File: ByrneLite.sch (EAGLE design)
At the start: 22 parts, among them J1 5V Reg, U1 TINY85, U2 S108T02, U3 S108T02, U4 S108T02

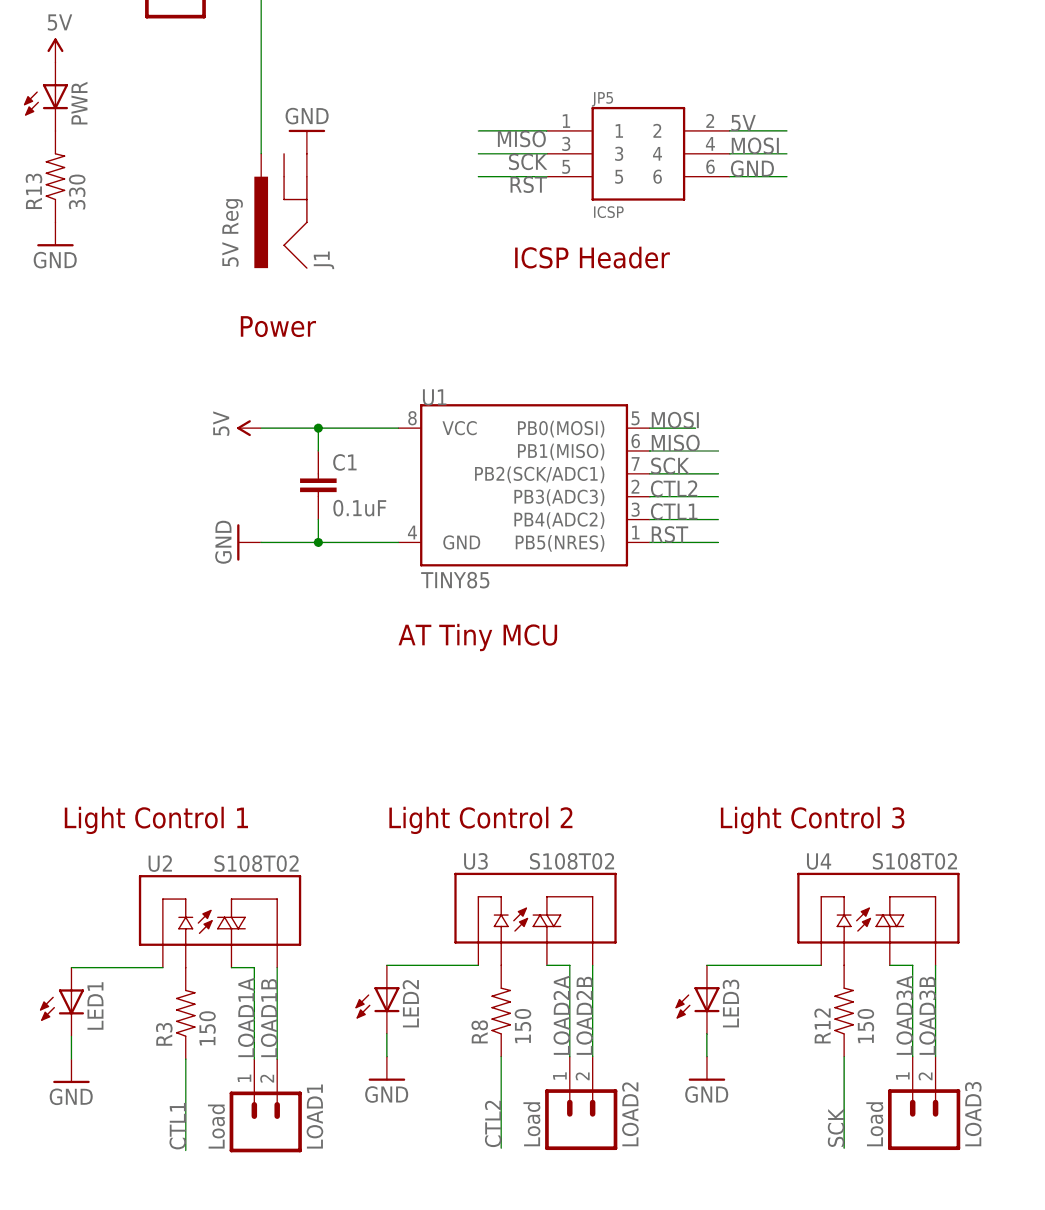
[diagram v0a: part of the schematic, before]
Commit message: Changed to LGPL license
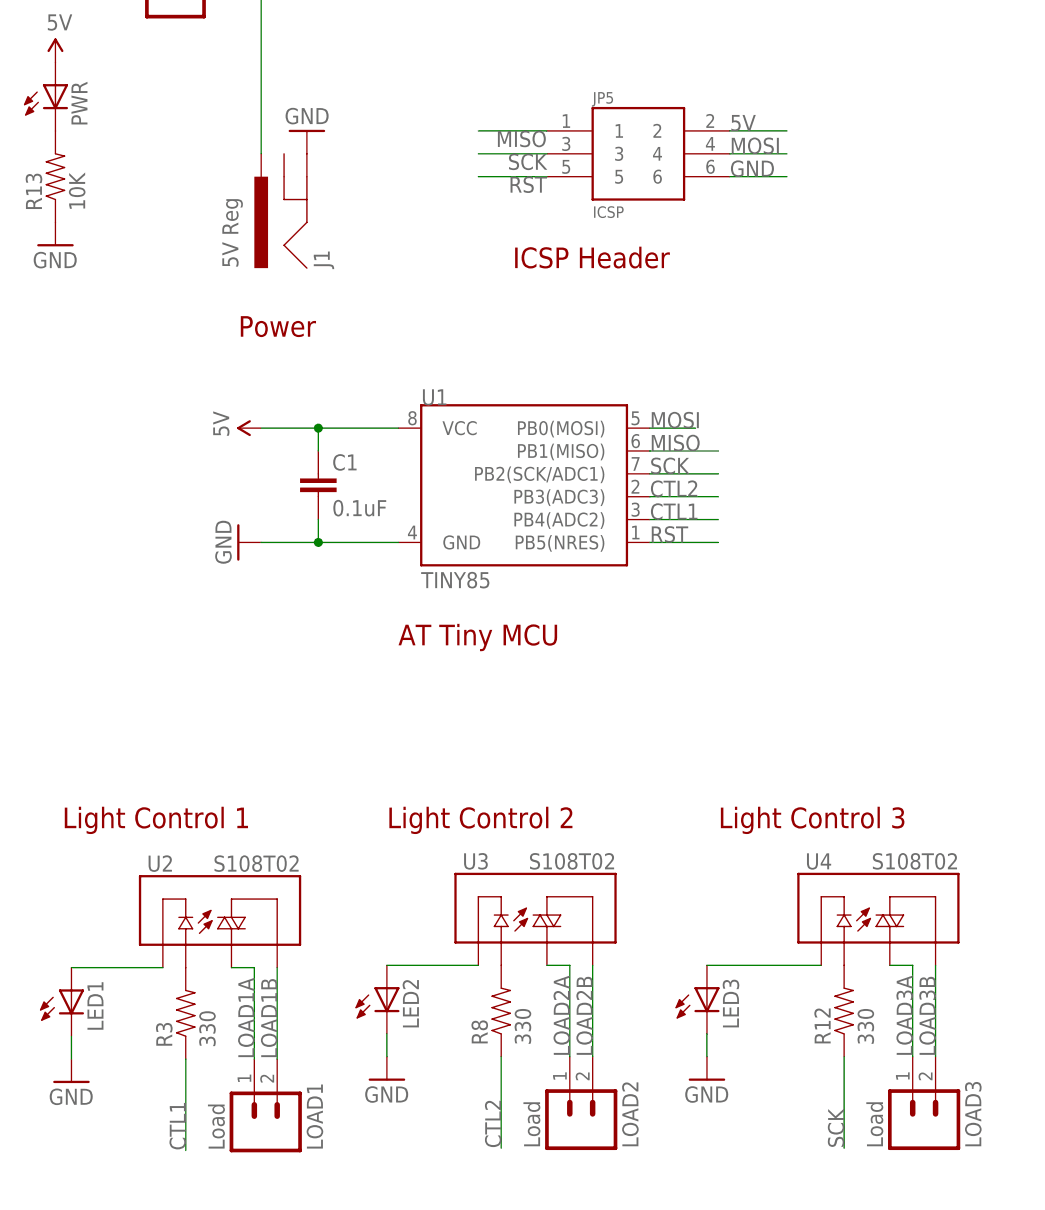
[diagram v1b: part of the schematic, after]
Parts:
- R12, R3, R8: value 150 -> 330
- R13: value 330 -> 10K
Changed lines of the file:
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@@
 <part name="FRAME1" library="SparkFun" deviceset="FRAME-LETTER" device=""/>
 <part name="LED1" library="SparkFun" deviceset="LED" device="5MM"/>
-<part name="R3" library="SparkFun" deviceset="RESISTOR" device="AXIAL-0.3" value="150"/>
+<part name="R3" library="SparkFun" deviceset="RESISTOR" device="AXIAL-0.3" value="330"/>
 <part name="U2" library="SparkFun" deviceset="RELAY-SOLIDSTATE" device="PTH" value="S108T02"/>
 <part name="LOAD1" library="SparkFun" deviceset="M02" device="5MM" value="Load"/>
@@
 <part name="GND2" library="SparkFun" deviceset="GND" device=""/>
 <part name="LED2" library="SparkFun" deviceset="LED" device="5MM"/>
-<part name="R8" library="SparkFun" deviceset="RESISTOR" device="AXIAL-0.3" value="150"/>
+<part name="R8" library="SparkFun" deviceset="RESISTOR" device="AXIAL-0.3" value="330"/>
 <part name="U3" library="SparkFun" deviceset="RELAY-SOLIDSTATE" device="PTH" value="S108T02"/>
 <part name="LOAD2" library="SparkFun" deviceset="M02" device="5MM" value="Load"/>
 <part name="LED3" library="SparkFun" deviceset="LED" device="5MM"/>
 <part name="GND7" library="SparkFun" deviceset="GND" device=""/>
-<part name="R12" library="SparkFun" deviceset="RESISTOR" device="AXIAL-0.3" value="150"/>
+<part name="R12" library="SparkFun" deviceset="RESISTOR" device="AXIAL-0.3" value="330"/>
 <part name="U4" library="SparkFun" deviceset="RELAY-SOLIDSTATE" device="PTH" value="S108T02"/>
 <part name="LOAD3" library="SparkFun" deviceset="M02" device="5MM" value="Load"/>
@@
 <part name="U$2" library="SparkFun" deviceset="5V" device=""/>
 <part name="PWR" library="SparkFun" deviceset="LED" device="3MM"/>
-<part name="R13" library="SparkFun" deviceset="RESISTOR" device="AXIAL-0.3" value="330"/>
+<part name="R13" library="SparkFun" deviceset="RESISTOR" device="AXIAL-0.3" value="10K"/>
 <part name="U$1" library="SparkFun" deviceset="5V" device=""/>
 <part name="GND8" library="SparkFun" deviceset="GND" device=""/>
